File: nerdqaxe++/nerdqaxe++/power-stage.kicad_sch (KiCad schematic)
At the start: 19 parts, among them U9 CSD95472Q5MC

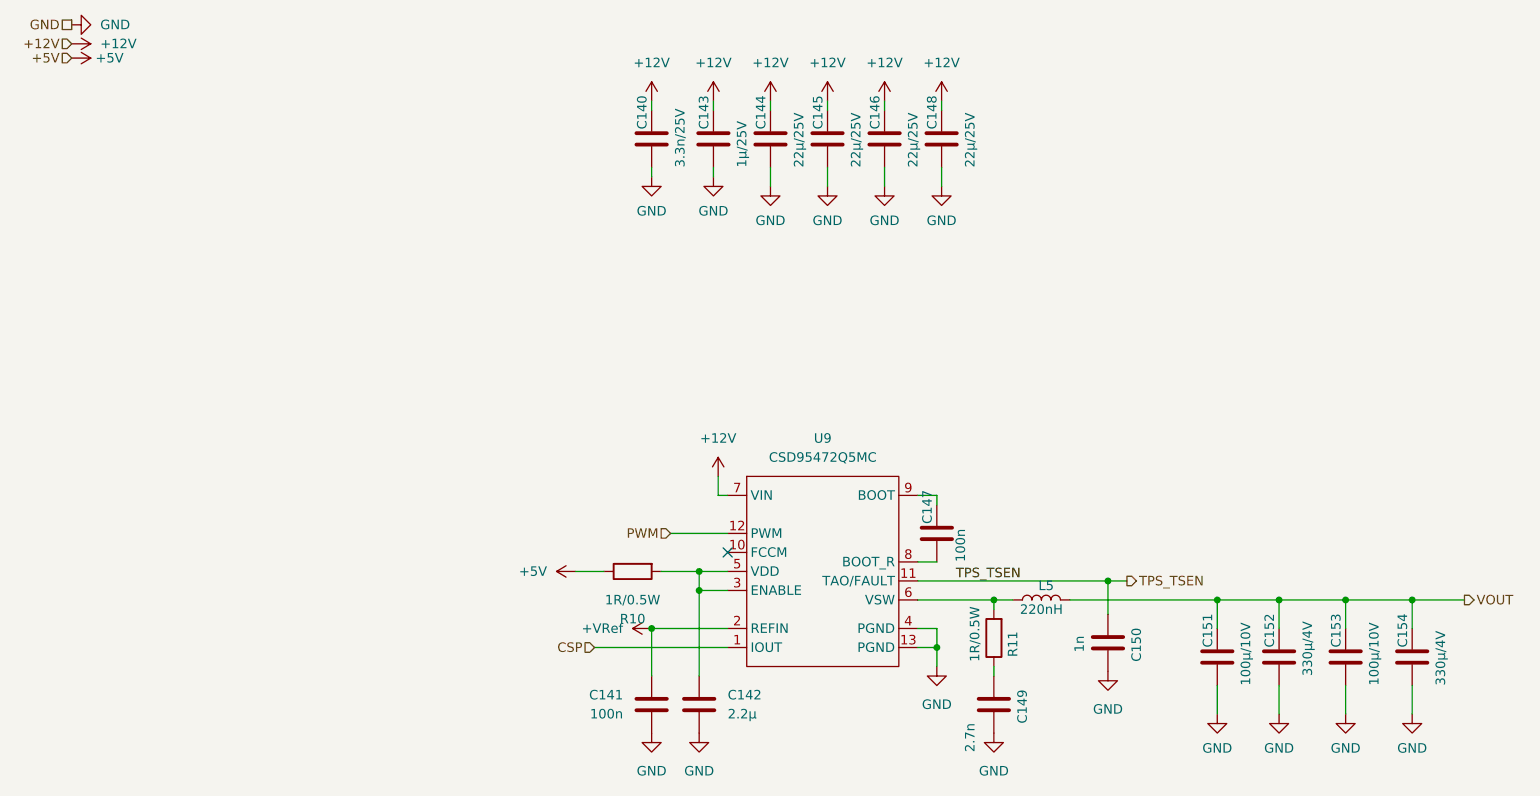
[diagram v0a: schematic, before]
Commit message: Nerdqaxe++ rev6.1.2PM
1. BM1370 Footprint solder paste revision
2. Added 2R2 resistor in series with bootstrap cap for CSD95472Q5MC
3. 180nH inductors for CSD
4. Vsense closer to ASICs
5. Fiducials
6. Updated top silkscreen
7. Various changes in tracing
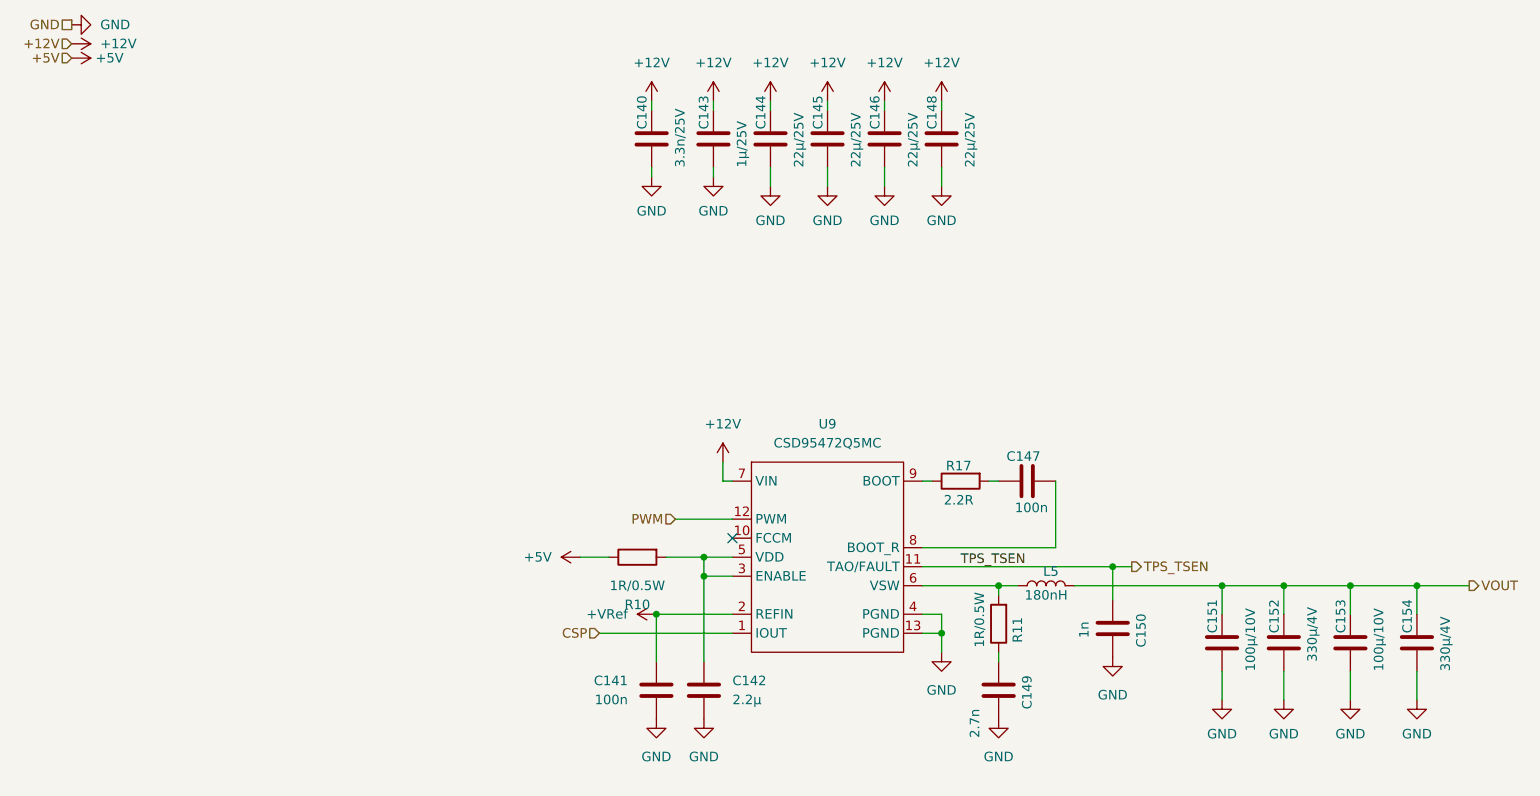
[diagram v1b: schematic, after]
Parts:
- added R17: 2.2R, Resistor_SMD:R_0603_1608Metric, symbol Device:R
- C147: footprint Capacitor_SMD:C_0805_2012Metric -> Capacitor_SMD:C_0603_1608Metric; Manufacturer C0805C104K5RACTU -> C0603C104K5RACTU; OrderNr 399-C0805C104K5RACTUCT-ND -> C0603C104K5RACTU
- L5: value 220nH -> 180nH; footprint myfootprints:IFLR-4031GC-01-8x10 -> qaxe:PA5187181HLT; Manufacturer FP1008R5-R220-R -> PA5187.181HLT; OrderNr 283-FP1008R5-R220-RCT-ND -> PA5187.181HLT
- U9: footprint myfootprints:CSD95472-SON-5x6 -> qaxe:CSD95472Q5MC
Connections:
- net at U9.9 (BOOT): now also R17.1; no longer C147.1
- new net: C147.1, R17.2
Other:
- moved on the sheet: C141, C142, C147, C149, C150, C151, C152, C153, C154, L5, R10, R11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
